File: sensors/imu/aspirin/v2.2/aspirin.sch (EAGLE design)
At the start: 24 parts, among them IC1 LP2992, IC2 MS5611, IC3 >4KBIT SERIAL EEPROM HALF PRO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, U1 HMC5883, U2 MPU-6000

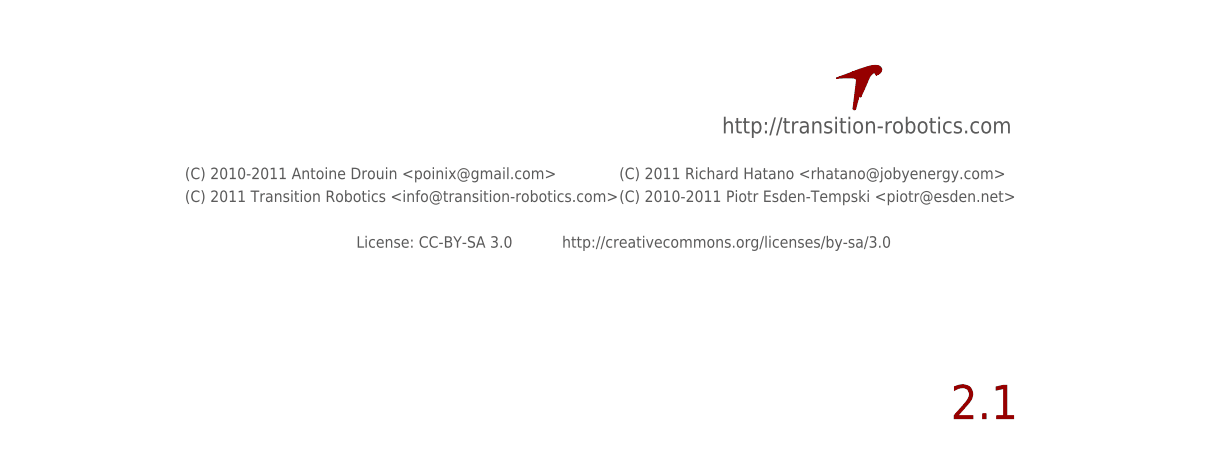
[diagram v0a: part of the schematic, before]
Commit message: Added panelization files to aspirin v2.2.
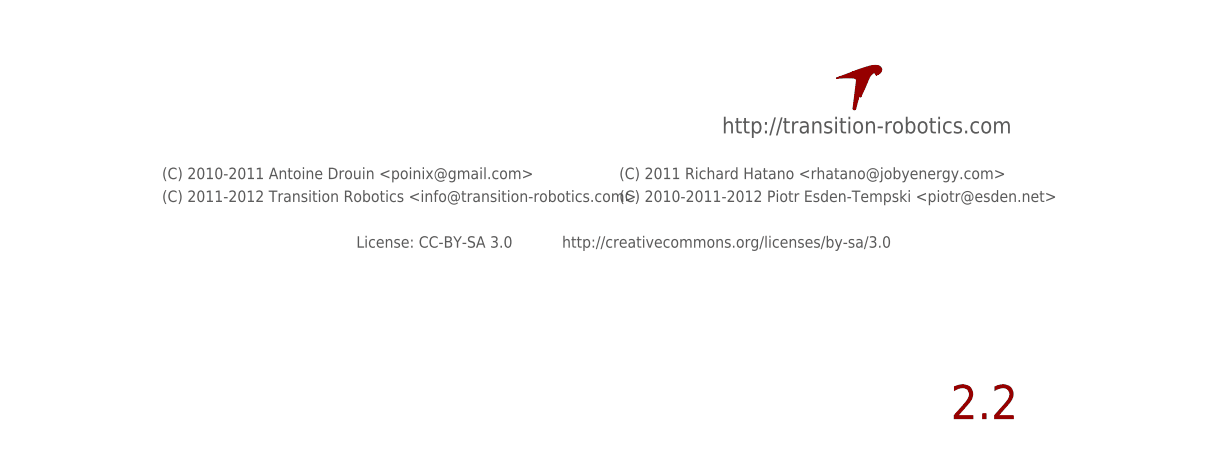
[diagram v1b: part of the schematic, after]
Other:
- note added: "(C) 2010-2011-2012 Piotr Esden-Tempski <piotr@esden.net>"
- note added: "(C) 2011-2012 Transition Robotics <info@transition-robotics.com>"
- note added: "2.2"
- note removed: "(C) 2010-2011 Piotr Esden-Tempski <piotr@esden.net>"
- note removed: "(C) 2011 Transition Robotics <info@transition-robotics.com>"
- note removed: "2.1"
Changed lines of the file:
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@@
 <text x="194.31" y="168.91" size="5.08" layer="91">Magnetometer</text>
 <text x="113.03" y="161.29" size="5.08" layer="91">Accelerometer</text>
-<text x="254" y="6.35" size="3.81" layer="94">2.1</text>
+<text x="254" y="6.35" size="3.81" layer="94">2.2</text>
 <text x="228.6" y="38.1" size="1.778" layer="97">http://transition-robotics.com</text>
 <text x="39.37" y="118.11" size="5.08" layer="91">Presure</text>
 <text x="187.96" y="25.4" size="1.27" layer="97">License: CC-BY-SA 3.0</text>
 <text x="210.82" y="25.4" size="1.27" layer="97">http://creativecommons.org/licenses/by-sa/3.0</text>
-<text x="217.17" y="30.48" size="1.27" layer="97">(C) 2010-2011 Piotr Esden-Tempski &lt;piotr@esden.net&gt;</text>
-<text x="168.91" y="33.02" size="1.27" layer="97">(C) 2010-2011 Antoine Drouin &lt;poinix@gmail.com&gt;</text>
+<text x="217.17" y="30.48" size="1.27" layer="97">(C) 2010-2011-2012 Piotr Esden-Tempski &lt;piotr@esden.net&gt;</text>
+<text x="166.37" y="33.02" size="1.27" layer="97">(C) 2010-2011 Antoine Drouin &lt;poinix@gmail.com&gt;</text>
 <text x="217.17" y="33.02" size="1.27" layer="97">(C) 2011 Richard Hatano &lt;rhatano@jobyenergy.com&gt;</text>
-<text x="168.91" y="30.48" size="1.27" layer="97">(C) 2011 Transition Robotics &lt;info@transition-robotics.com&gt;</text>
+<text x="166.37" y="30.48" size="1.27" layer="97">(C) 2011-2012 Transition Robotics &lt;info@transition-robotics.com&gt;</text>
 </plain>
 <instances>

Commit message: Minor touchups.
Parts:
- L1: PARTNO MMZ1608B601C -> ferrite-0603-600ohm
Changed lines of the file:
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@@
 </part>
 <part name="L1" library="res_cap" deviceset="INDUCTOR" device="-0603" value="">
-<attribute name="PARTNO" value="MMZ1608B601C"/>
+<attribute name="PARTNO" value="ferrite-0603-600ohm"/>
 </part>
 </parts>

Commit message: Updated aspirin v2.2 to r1
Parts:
- removed U$1: TR-LOGO, quadshot:TR-LOGO
- added U$2: 1B2-NEW-LOGO-3MM, 1b2:1B2-NEW-LOGO-3MM
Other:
- note added: "(C) 2010-2013 Piotr Esden-Tempski <piotr@esden.net>"
- note added: "(C) 2013 1BitSquared <info@1bitsquared.com>"
- note added: "1 BIT SQUARED"
- note removed: "(C) 2010-2011-2012 Piotr Esden-Tempski <piotr@esden.net>"
- note removed: "http://transition-robotics.com"
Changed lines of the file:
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@@
 <?xml version="1.0" encoding="utf-8"?>
 <!DOCTYPE eagle SYSTEM "eagle.dtd">
-<eagle version="6.2">
+<eagle version="6.4">
 <drawing>
 <settings>
@@
 <layer number="144" name="DrillLegend" color="7" fill="1" visible="yes" active="yes"/>
 <layer number="151" name="HeatSink" color="7" fill="1" visible="yes" active="yes"/>
+<layer number="199" name="Contour" color="7" fill="1" visible="yes" active="yes"/>
 <layer number="200" name="200bmp" color="1" fill="10" visible="no" active="no"/>
 <layer number="201" name="201bmp" color="2" fill="1" visible="no" active="no"/>
@@
 <layer number="207" name="207bmp" color="8" fill="10" visible="yes" active="yes"/>
 <layer number="208" name="208bmp" color="9" fill="10" visible="yes" active="yes"/>
+<layer number="209" name="209bmp" color="7" fill="1" visible="yes" active="yes"/>
+<layer number="210" name="210bmp" color="7" fill="1" visible="yes" active="yes"/>
+<layer number="211" name="211bmp" color="7" fill="1" visible="yes" active="yes"/>
+<layer number="212" name="212bmp" color="7" fill="1" visible="yes" active="yes"/>
+<layer number="213" name="213bmp" color="7" fill="1" visible="yes" active="yes"/>
+<layer number="214" name="214bmp" color="7" fill="1" visible="yes" active="yes"/>
+<layer number="215" name="215bmp" color="7" fill="1" visible="yes" active="yes"/>
+<layer number="216" name="216bmp" color="7" fill="1" visible="yes" active="yes"/>
+<layer number="217" name="217bmp" color="18" fill="1" visible="no" active="no"/>
+<layer number="218" name="218bmp" color="19" fill="1" visible="no" active="no"/>
+<layer number="219" name="219bmp" color="20" fill="1" visible="no" active="no"/>
+<layer number="220" name="220bmp" color="21" fill="1" visible="no" active="no"/>
+<layer number="221" name="221bmp" color="22" fill="1" visible="no" active="no"/>
+<layer number="222" name="222bmp" color="23" fill="1" visible="no" active="no"/>
+<layer number="223" name="223bmp" color="24" fill="1" visible="no" active="no"/>
+<layer number="224" name="224bmp" color="25" fill="1" visible="no" active="no"/>
 <layer number="231" name="Eagle3D_PG1" color="14" fill="1" visible="yes" active="yes"/>
 <layer number="232" name="Eagle3D_PG2" color="14" fill="2" visible="yes" active="yes"/>
@@
 </part>
 <part name="GND3" library="supply1" deviceset="GND" device=""/>
-<part name="U$1" library="quadshot" deviceset="TR-LOGO" device="">
-<attribute name="BOM" value="EXCLUDE"/>
-<attribute name="PARTNO" value="*"/>
-</part>
 <part name="JP5" library="pel_jumpers" deviceset="SQ_JMP" device="-0402" value="0/DNP">
 <attribute name="DNP" value="T"/>
@@
 <part name="L1" library="res_cap" deviceset="INDUCTOR" device="-0603" value="">
 <attribute name="PARTNO" value="ferrite-0603-600ohm"/>
+</part>
+<part name="U$2" library="1b2" deviceset="1B2-NEW-LOGO" device="-3MM" value="1B2-NEW-LOGO-3MM">
+<attribute name="BOM" value="EXCLUDE"/>
 </part>
 </parts>
@@
 <text x="113.03" y="161.29" size="5.08" layer="91">Accelerometer</text>
 <text x="254" y="6.35" size="3.81" layer="94">2.2</text>
-<text x="228.6" y="38.1" size="1.778" layer="97">http://transition-robotics.com</text>
 <text x="39.37" y="118.11" size="5.08" layer="91">Presure</text>
 <text x="187.96" y="25.4" size="1.27" layer="97">License: CC-BY-SA 3.0</text>
 <text x="210.82" y="25.4" size="1.27" layer="97">http://creativecommons.org/licenses/by-sa/3.0</text>
-<text x="217.17" y="30.48" size="1.27" layer="97">(C) 2010-2011-2012 Piotr Esden-Tempski &lt;piotr@esden.net&gt;</text>
-<text x="166.37" y="33.02" size="1.27" layer="97">(C) 2010-2011 Antoine Drouin &lt;poinix@gmail.com&gt;</text>
+<text x="217.17" y="30.48" size="1.27" layer="97">(C) 2010-2013 Piotr Esden-Tempski &lt;piotr@esden.net&gt;</text>
+<text x="163.83" y="33.02" size="1.27" layer="97">(C) 2010-2011 Antoine Drouin &lt;poinix@gmail.com&gt;</text>
 <text x="217.17" y="33.02" size="1.27" layer="97">(C) 2011 Richard Hatano &lt;rhatano@jobyenergy.com&gt;</text>
-<text x="166.37" y="30.48" size="1.27" layer="97">(C) 2011-2012 Transition Robotics &lt;info@transition-robotics.com&gt;</text>
+<text x="163.83" y="30.48" size="1.27" layer="97">(C) 2011-2012 Transition Robotics &lt;info@transition-robotics.com&gt;</text>
+<text x="208.28" y="40.64" size="2.54" layer="111">1 BIT SQUARED</text>
+<text x="217.17" y="27.94" size="1.27" layer="97">(C) 2013 1BitSquared &lt;info@1bitsquared.com&gt;</text>
 </plain>
 <instances>
@@
 </instance>
 <instance part="GND3" gate="1" x="91.44" y="40.64" rot="MR0"/>
-<instance part="U$1" gate="G$1" x="243.84" y="43.18">
-<attribute name="PARTNO" x="243.84" y="43.18" size="1.778" layer="96" rot="MR0" display="off"/>
-<attribute name="BOM" x="243.84" y="43.18" size="1.778" layer="96" rot="R180" display="off"/>
-</instance>
 <instance part="JP5" gate="G$1" x="149.86" y="88.9">
 <attribute name="PARTNO" value="res-0402-0" x="149.86" y="88.9" size="1.778" layer="96" rot="MR90" display="off"/>
@@
 <attribute name="PARTNO" x="20.32" y="101.6" size="1.778" layer="96" rot="MR270" display="off"/>
 </instance>
+<instance part="U$2" gate="G$1" x="195.58" y="38.1">
+<attribute name="BOM" x="195.58" y="38.1" size="1.778" layer="96" rot="R180" display="off"/>
+</instance>
 </instances>
